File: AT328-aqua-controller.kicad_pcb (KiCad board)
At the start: 2 copper layers, 76.6 x 76 mm, 41 parts, among them J1 LED-Strip, J2 Fan, J3 Display, J4 FTDI, J5 Temp, J6 12/24v, Q1 IRL520N, Q2 IRL520N, Q3 IRL520N, Q4 IRL520N, Q5 BC547, SW1 Lid Open, SW2 Lights/Cycle, U1 ATmega328P-PU, U2 LM7805_TO220, Y1 16MHz

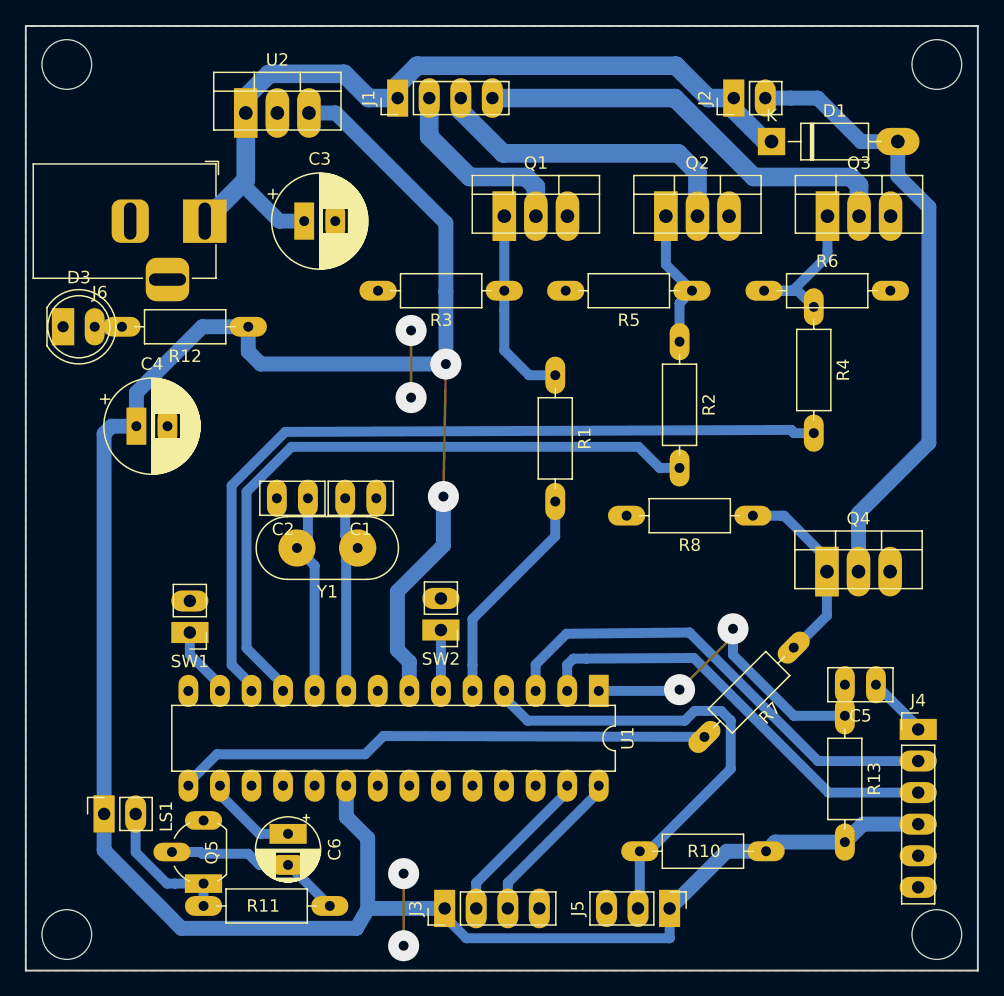
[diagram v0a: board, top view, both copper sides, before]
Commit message: More IO and better PCB silk
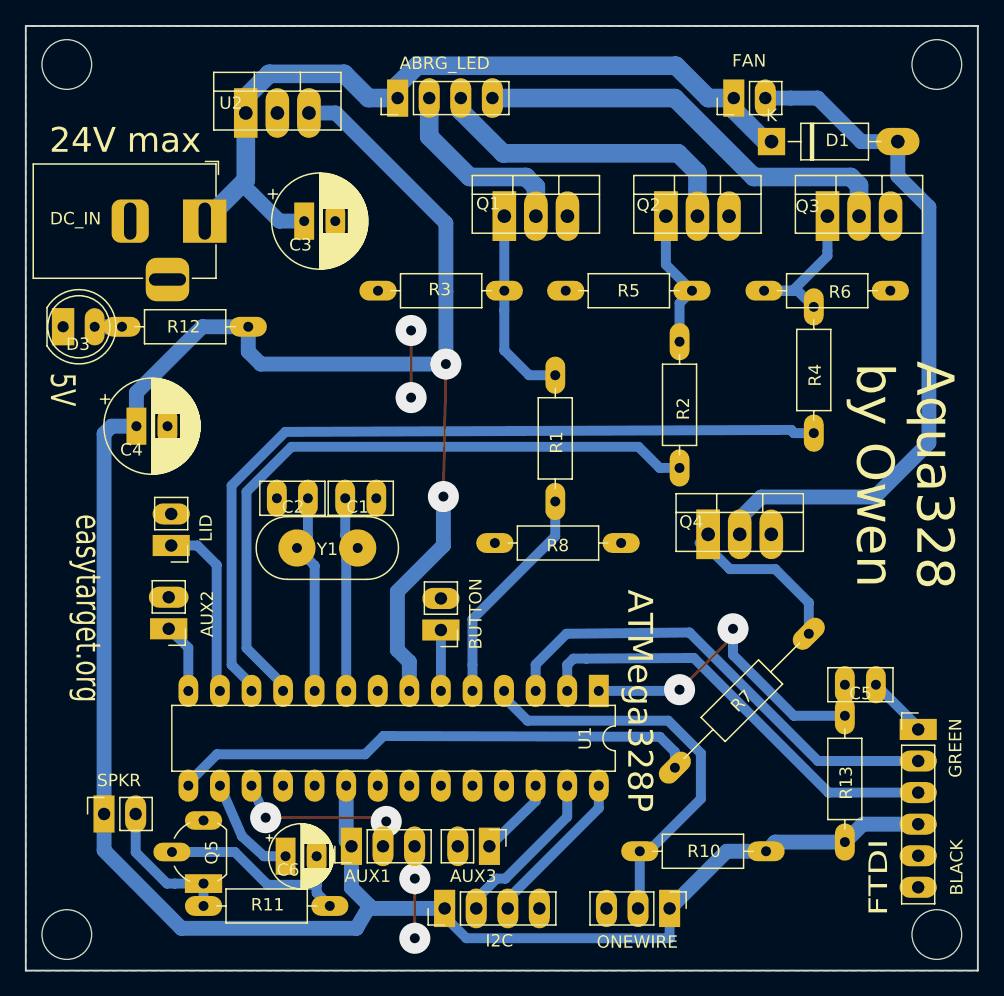
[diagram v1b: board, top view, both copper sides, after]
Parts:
- removed J2: Fan, Connector_PinHeader_2.54mm:PinHeader_1x02_P2.54mm_Vertical
- removed J3: Display, Connector_PinHeader_2.54mm:PinHeader_1x04_P2.54mm_Vertical
- removed J4: FTDI, Connector_PinHeader_2.54mm:PinHeader_1x06_P2.54mm_Vertical
- removed J6: 12/24v, Connector_BarrelJack:BarrelJack_Horizontal
- removed LS1: Speaker, Connector_PinSocket_2.54mm:PinSocket_1x02_P2.54mm_Vertical
- removed SW1: Lid Open, Connector_PinHeader_2.54mm:PinHeader_1x02_P2.54mm_Vertical
- added AUX1: Aux Connector, Connector_PinHeader_2.54mm:PinHeader_1x03_P2.54mm_Vertical, F.Cu at (58.0, 93.5)
- added AUX2: Aux Connector, Connector_PinHeader_2.54mm:PinHeader_1x02_P2.54mm_Vertical, F.Cu at (43.3, 76.0)
- added AUX3: Aux Connector, Connector_PinHeader_2.54mm:PinHeader_1x02_P2.54mm_Vertical, F.Cu at (69.1, 93.5)
- added DC_IN: 12/24v, Connector_BarrelJack:BarrelJack_Horizontal, F.Cu at (46.2, 43.2)
- added FAN: Fan PWM NPN, Connector_PinHeader_2.54mm:PinHeader_1x02_P2.54mm_Vertical, F.Cu at (88.8, 33.3)
- added FTDI: FTDI Program Port, Connector_PinHeader_2.54mm:PinHeader_1x06_P2.54mm_Vertical, F.Cu at (103.6, 84.1)
- added I2C: Display, Connector_PinHeader_2.54mm:PinHeader_1x04_P2.54mm_Vertical, F.Cu at (65.5, 98.5)
- added LID: Lid Open, Connector_PinHeader_2.54mm:PinHeader_1x02_P2.54mm_Vertical, F.Cu at (43.5, 69.3)
- added SPKR: Speaker, Connector_PinSocket_2.54mm:PinSocket_1x02_P2.54mm_Vertical, F.Cu at (38.1, 90.9)
- R7: footprint Resistor_THT:R_Axial_DIN0207_L6.3mm_D2.5mm_P10.16mm_Horizontal -> Resistor_THT:R_Axial_DIN0207_L6.3mm_D2.5mm_P15.24mm_Horizontal
- moved R8 10.8 mm to (79.7, 69.1)
- moved Q4 10.0 mm to (86.7, 68.4)
- moved C6 1.81 mm to (52.7, 94.3), turned to 0 degrees
- moved R7 1.65 mm to (94.8, 76.4)
- renumbered J1 to ABRG_LED, SW2 to BUTTON, J5 to ONEWIRE
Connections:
- U1 pad 14: (no net) -> AUX2
- U1 pad 17: (no net) -> AUX1
- U1 pad 26: (no net) -> AUX3
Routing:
- net AUX1: track 0.00 -> 14.8 mm, vias 0 -> 2
- net LID: track 5.70 -> 14.6 mm
- net AUX3: track 0.00 -> 6.45 mm
- net Net-(D1-Pad2): track 50.1 -> 56.4 mm
- net AUX2: track 0.00 -> 5.67 mm
- net 1WIRE: track 38.8 -> 33.2 mm
- net Net-(C6-Pad2): track 15.3 -> 19.5 mm
- net BUZZ: track 7.50 -> 8.57 mm
- net GND: track 11.2 -> 10.2 mm
- net SDA: track 13.7 -> 12.9 mm
- net FAN: track 44.3 -> 43.7 mm
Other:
- board text added: "24V max"
- board text added: "5V"
- board text added: "ATMega328P"
- board text added: "Aqua328 by Owen"
- board text added: "easytarget.org"

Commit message: More PCB work, adding power to all pins, more io and better silk
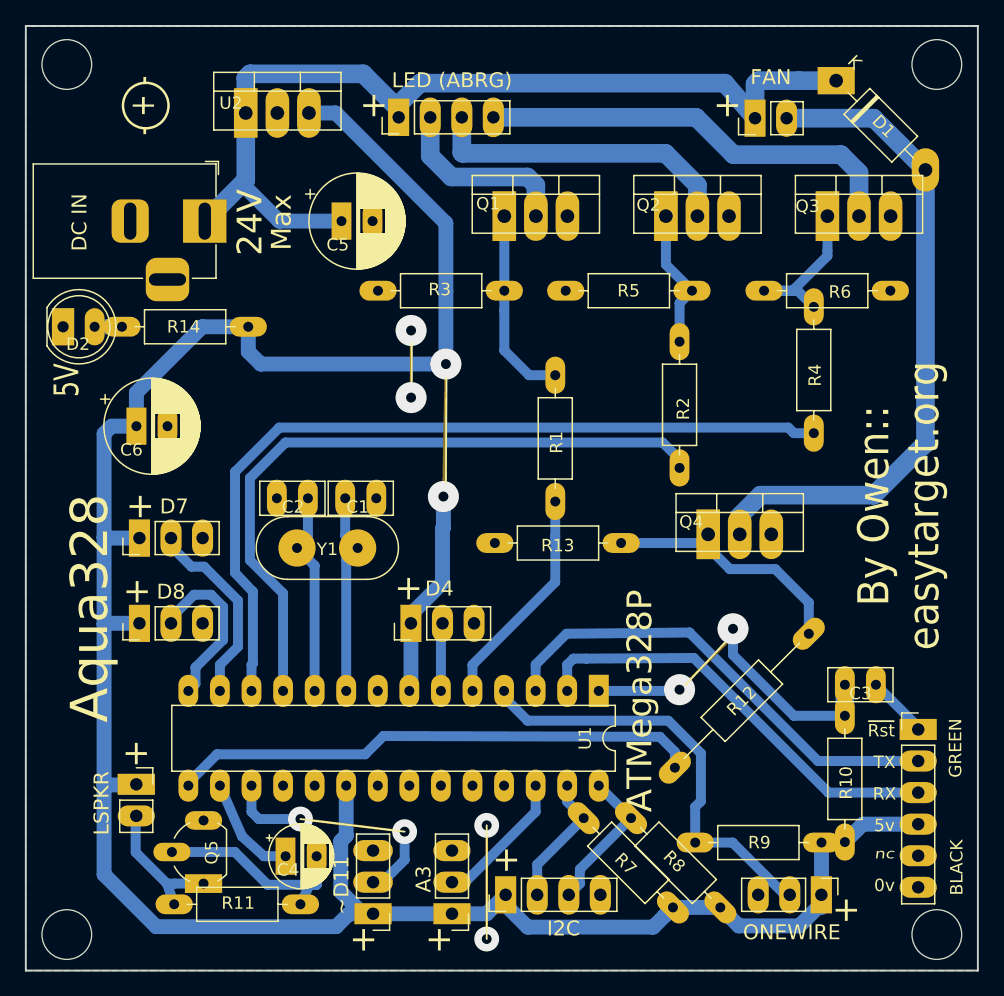
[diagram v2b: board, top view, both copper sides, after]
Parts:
- removed BUTTON: Lights/Cycle, Connector_PinHeader_2.54mm:PinHeader_1x02_P2.54mm_Vertical
- removed the C6 at (52.7, 94.3)
- removed DC_IN: 12/24v, Connector_BarrelJack:BarrelJack_Horizontal
- removed FAN: Fan PWM NPN, Connector_PinHeader_2.54mm:PinHeader_1x02_P2.54mm_Vertical
- removed FTDI: FTDI Program Port, Connector_PinHeader_2.54mm:PinHeader_1x06_P2.54mm_Vertical
- removed LID: Lid Open, Connector_PinHeader_2.54mm:PinHeader_1x02_P2.54mm_Vertical
- removed the R10 at (91.4, 93.9)
- removed SPKR: Speaker, Connector_PinSocket_2.54mm:PinSocket_1x02_P2.54mm_Vertical
- added BUTTON1: Lights/Cycle, Connector_PinHeader_2.54mm:PinHeader_1x03_P2.54mm_Vertical, F.Cu at (62.8, 75.6)
- added C4: 47uF, Capacitor_THT:CP_Radial_D5.0mm_P2.50mm, F.Cu at (52.7, 94.3)
- added DC_IN1: 12/24v, Connector_BarrelJack:BarrelJack_Horizontal, F.Cu at (46.2, 43.2)
- added FAN1: Fan PWM NPN, Connector_PinHeader_2.54mm:PinHeader_1x02_P2.54mm_Vertical, F.Cu at (90.5, 34.9)
- added FTDI1: FTDI Program Port, Connector_PinHeader_2.54mm:PinHeader_1x06_P2.54mm_Vertical, F.Cu at (103.6, 84.1)
- added LID1: Lid Open, Connector_PinHeader_2.54mm:PinHeader_1x03_P2.54mm_Vertical, F.Cu at (40.9, 68.7)
- added R7: 4K7, Resistor_THT:R_Axial_DIN0207_L6.3mm_D2.5mm_P10.16mm_Horizontal, F.Cu at (83.9, 98.4)
- added R8: 4K7, Resistor_THT:R_Axial_DIN0207_L6.3mm_D2.5mm_P10.16mm_Horizontal, F.Cu at (87.7, 98.4)
- added R9: 4K7, Resistor_THT:R_Axial_DIN0207_L6.3mm_D2.5mm_P10.16mm_Horizontal, F.Cu at (95.8, 93.2)
- added SPKR1: Speaker, Connector_PinSocket_2.54mm:PinSocket_1x02_P2.54mm_Vertical, F.Cu at (40.7, 88.5)
- AUX2, AUX3: footprint Connector_PinHeader_2.54mm:PinHeader_1x02_P2.54mm_Vertical -> Connector_PinHeader_2.54mm:PinHeader_1x03_P2.54mm_Vertical
- moved AUX3 33.4 mm to (40.9, 75.6), turned to 90 degrees
- moved AUX2 32.3 mm to (66.1, 98.9)
- moved ONEWIRE1 12.3 mm to (95.8, 97.4)
- moved D1 7.14 mm to (97.0, 31.9), turned to 315 degrees
- moved AUX1 5.70 mm to (59.7, 98.9), turned to 180 degrees
- moved I2C1 5.03 mm to (70.4, 97.4)
- moved C5 3.00 mm to (57.2, 43.2)
- moved R11 2.37 mm to (43.7, 98.2)
- moved ABRG_LED1 1.55 mm to (61.8, 34.9)
- renumbered ABRG_LED to ABRG_LED1, C5 to C3, C3 to C5, C4 to C6, D3 to D2, I2C to I2C1, ONEWIRE to ONEWIRE1, R13 to R10, R7 to R12, R8 to R13, R12 to R14
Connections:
- AUX2 pad 1: AUX2 -> +5V
- AUX2 pad 2: GND -> AUX2
- AUX3 pad 1: AUX3 -> +5V
- AUX3 pad 2: GND -> AUX3
- U1 pad 14: AUX2 -> AUX3
- U1 pad 26: AUX3 -> AUX2
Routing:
- net +5V: track 209.1 -> 222.9 mm
- net +VDC: track 67.4 -> 77.7 mm
- net AUX3: track 6.45 -> 13.7 mm
- net Net-(Q4-Pad1): track 14.5 -> 20.8 mm
- net AUX1: track 14.8 -> 20.3 mm
- net AUX2: track 5.67 -> 11.2 mm
- net GND: track 10.2 -> 14.5 mm
- net SCL: track 13.8 -> 10.9 mm
- net Net-(D1-Pad2): track 56.4 -> 53.7 mm
- net 1WIRE: track 33.2 -> 35.7 mm
- net Net-(C4-Pad2): track 19.5 -> 17.3 mm
- net LID: track 14.6 -> 15.7 mm
- net SDA: track 12.9 -> 11.9 mm
- net LED-R: track 54.3 -> 55.2 mm
- net Net-(ABRG_LED1-Pad2): track 15.7 -> 15.1 mm
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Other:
- board text added: "24V"
- board text added: "Aqua328"
- board text added: "By Owen:: easytarget.org"
- board text added: "Max"
- board text removed: "24V max"
- board text removed: "Aqua328 by Owen"
- board text removed: "easytarget.org"

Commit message: Bigger power terminals, all power wiring on one side, bigger power tracks
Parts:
- ABRG_LED1: footprint Connector_PinHeader_2.54mm:PinHeader_1x04_P2.54mm_Vertical -> TerminalBlock:TerminalBlock_bornier-4_P5.08mm
- FAN1: footprint Connector_PinHeader_2.54mm:PinHeader_1x02_P2.54mm_Vertical -> TerminalBlock:TerminalBlock_bornier-2_P5.08mm
- moved DC_IN1 3.98 mm to (42.7, 41.3), turned to 270 degrees
- moved U2 3.62 mm to (52.4, 36.7)
- moved FAN1 3.56 mm to (86.9, 34.9), turned to 0 degrees
- moved ABRG_LED1 3.02 mm to (64.8, 34.9), turned to 0 degrees
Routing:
- net Net-(ABRG_LED1-Pad4): track 34.8 -> 24.1 mm
- net +VDC: track 77.7 -> 68.6 mm
- net Net-(ABRG_LED1-Pad3): track 25.4 -> 17.2 mm
- net Net-(ABRG_LED1-Pad2): track 15.1 -> 9.17 mm
- net +5V: track 222.9 -> 218.6 mm
- net Net-(D1-Pad2): track 53.7 -> 54.8 mm

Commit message: Lots of minor tweaks to layout and silkscreen, possibly complete.
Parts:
- D1: footprint Diode_THT:D_DO-41_SOD81_P10.16mm_Horizontal -> Diode_THT:D_DO-41_SOD81_P2.54mm_Vertical_KathodeUp
- moved R14 26.5 mm to (38.1, 75.6), turned to 90 degrees
- moved C5 17.2 mm to (41.0, 48.9)
- moved D1 3.84 mm to (99.4, 34.9), turned to 180 degrees
- moved D2 2.92 mm to (37.1, 53.5), turned to 270 degrees
- moved R9 1.44 mm to (94.5, 93.8), turned to 135 degrees
- moved R3 1.38 mm to (71.7, 48.8)
- moved C6 0.91 mm to (40.9, 60.6)
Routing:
- net Net-(D2-Pad2): track 2.20 -> 9.82 mm
- net +VDC: track 68.6 -> 75.1 mm
- net +5V: track 218.6 -> 213.9 mm
- net 1WIRE: track 35.7 -> 33.6 mm
- net Net-(D1-Pad2): track 54.8 -> 55.5 mm
- net Net-(ABRG_LED1-Pad4): track 24.1 -> 23.5 mm
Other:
- board text added: "7805"
- board text added: "By Owen @ easytarget.org"
- board text added: "D2"
- board text added: "~~D10"
- board text added: "~~D3"
- board text added: "~~D5"
- board text added: "~~D6"
- board text added: "~~D9"
- board text removed: "By Owen:: easytarget.org"

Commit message: Add a version to silkscreen
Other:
- board text added: "v1.3"
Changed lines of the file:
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@@
   (general
     (thickness 1.6)
-    (drawings 37)
+    (drawings 38)
     (tracks 264)
     (zones 0)
@@
     )
   )
+  (gr_text v1.3 (at 100.634 53.97 90) (layer F.SilkS)
+    (effects (font (size 1 1) (thickness 0.1)))
+  )
   (gr_text D2 (at 93.014 95.118) (layer F.SilkS)
